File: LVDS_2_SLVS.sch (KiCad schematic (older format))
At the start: 6 parts

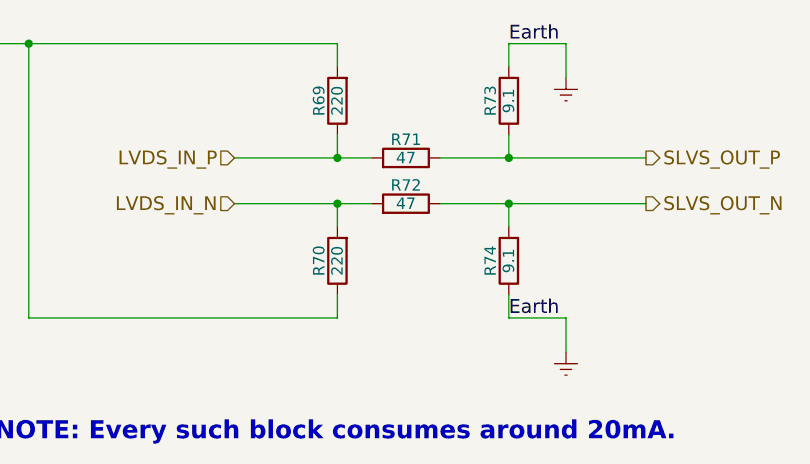
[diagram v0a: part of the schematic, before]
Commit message: Adding more LVDS lines
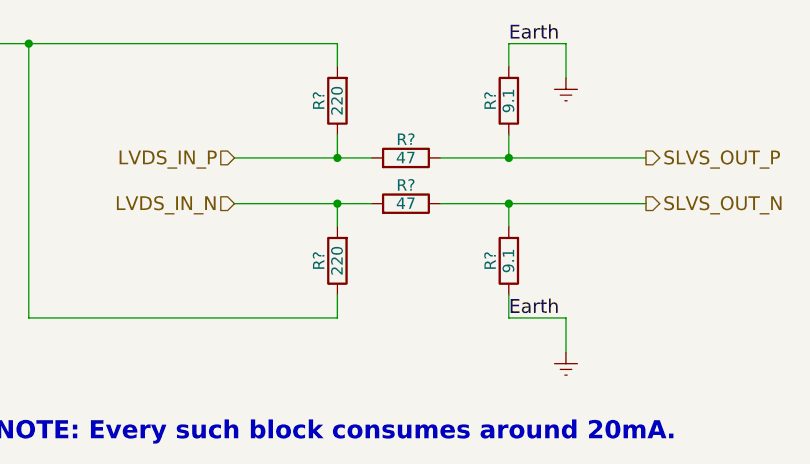
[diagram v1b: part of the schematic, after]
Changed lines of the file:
@@
 $Descr A4 11693 8268
 encoding utf-8
-Sheet 10 12
+Sheet 10 19
 Title ""
 Date ""
@@
 AR Path="/6191D89C/63D3885E/5955E861" Ref="R63"  Part="1"
 AR Path="/6191D89C/63D47A03/5955E861" Ref="R69"  Part="1"
-F 0 "R69" V 2680 1250 50  0000 C CNN
+AR Path="/6366AF3A/63C53CD1/5955E861" Ref="R?"  Part="1"
+AR Path="/6366AF3A/63D0A579/5955E861" Ref="R?"  Part="1"
+AR Path="/6366AF3A/63D1A4B4/5955E861" Ref="R?"  Part="1"
+AR Path="/6366AF3A/63D296AD/5955E861" Ref="R?"  Part="1"
+AR Path="/6366AF3A/63D3885E/5955E861" Ref="R?"  Part="1"
+AR Path="/6366AF3A/63D47A03/5955E861" Ref="R?"  Part="1"
+F 0 "R?" V 2680 1250 50  0000 C CNN
 F 1 "220" V 2600 1250 50  0000 C CNN
 F 2 "Resistors_SMD:R_0603" V 2530 1250 50  0001 C CNN
@@
 AR Path="/6191D89C/63D3885E/5955F5C4" Ref="R66"  Part="1"
 AR Path="/6191D89C/63D47A03/5955F5C4" Ref="R72"  Part="1"
-F 0 "R72" V 2980 1700 50  0000 C CNN
+AR Path="/6366AF3A/63C53CD1/5955F5C4" Ref="R?"  Part="1"
+AR Path="/6366AF3A/63D0A579/5955F5C4" Ref="R?"  Part="1"
+AR Path="/6366AF3A/63D1A4B4/5955F5C4" Ref="R?"  Part="1"
+AR Path="/6366AF3A/63D296AD/5955F5C4" Ref="R?"  Part="1"
+AR Path="/6366AF3A/63D3885E/5955F5C4" Ref="R?"  Part="1"
+AR Path="/6366AF3A/63D47A03/5955F5C4" Ref="R?"  Part="1"
+F 0 "R?" V 2980 1700 50  0000 C CNN
 F 1 "47" V 2900 1700 50  0000 C CNN
 F 2 "Resistors_SMD:R_0603" V 2830 1700 50  0001 C CNN
@@
 AR Path="/6191D89C/63D3885E/61C6D193" Ref="#PWR0125"  Part="1"
 AR Path="/6191D89C/63D47A03/61C6D193" Ref="#PWR0127"  Part="1"
-F 0 "#PWR0127" H 3600 2100 50  0001 C CNN
+AR Path="/6366AF3A/63C53CD1/61C6D193" Ref="#PWR?"  Part="1"
+AR Path="/6366AF3A/63D0A579/61C6D193" Ref="#PWR?"  Part="1"
+AR Path="/6366AF3A/63D1A4B4/61C6D193" Ref="#PWR?"  Part="1"
+AR Path="/6366AF3A/63D296AD/61C6D193" Ref="#PWR?"  Part="1"
+AR Path="/6366AF3A/63D3885E/61C6D193" Ref="#PWR?"  Part="1"
+AR Path="/6366AF3A/63D47A03/61C6D193" Ref="#PWR?"  Part="1"
+F 0 "#PWR?" H 3600 2100 50  0001 C CNN
 F 1 "Earth" H 3600 2200 50  0001 C CNN
 F 2 "" H 3600 2350 50  0000 C CNN
@@
 AR Path="/6191D89C/63D3885E/61C6D191" Ref="#PWR0126"  Part="1"
 AR Path="/6191D89C/63D47A03/61C6D191" Ref="#PWR0128"  Part="1"
-F 0 "#PWR0128" H 3600 900 50  0001 C CNN
+AR Path="/6366AF3A/63C53CD1/61C6D191" Ref="#PWR?"  Part="1"
+AR Path="/6366AF3A/63D0A579/61C6D191" Ref="#PWR?"  Part="1"
+AR Path="/6366AF3A/63D1A4B4/61C6D191" Ref="#PWR?"  Part="1"
+AR Path="/6366AF3A/63D296AD/61C6D191" Ref="#PWR?"  Part="1"
+AR Path="/6366AF3A/63D3885E/61C6D191" Ref="#PWR?"  Part="1"
+AR Path="/6366AF3A/63D47A03/61C6D191" Ref="#PWR?"  Part="1"
+F 0 "#PWR?" H 3600 900 50  0001 C CNN
 F 1 "Earth" H 3600 1000 50  0001 C CNN
 F 2 "" H 3600 1150 50  0000 C CNN
@@
 AR Path="/6191D89C/63D3885E/61C6D194" Ref="R64"  Part="1"
 AR Path="/6191D89C/63D47A03/61C6D194" Ref="R70"  Part="1"
-F 0 "R70" V 2680 1950 50  0000 C CNN
+AR Path="/6366AF3A/63C53CD1/61C6D194" Ref="R?"  Part="1"
+AR Path="/6366AF3A/63D0A579/61C6D194" Ref="R?"  Part="1"
+AR Path="/6366AF3A/63D1A4B4/61C6D194" Ref="R?"  Part="1"
+AR Path="/6366AF3A/63D296AD/61C6D194" Ref="R?"  Part="1"
+AR Path="/6366AF3A/63D3885E/61C6D194" Ref="R?"  Part="1"
+AR Path="/6366AF3A/63D47A03/61C6D194" Ref="R?"  Part="1"
+F 0 "R?" V 2680 1950 50  0000 C CNN
 F 1 "220" V 2600 1950 50  0000 C CNN
 F 2 "Resistors_SMD:R_0603" V 2530 1950 50  0001 C CNN
@@
 AR Path="/6191D89C/63D3885E/61C6D195" Ref="R65"  Part="1"
 AR Path="/6191D89C/63D47A03/61C6D195" Ref="R71"  Part="1"
-F 0 "R71" V 2980 1500 50  0000 C CNN
+AR Path="/6366AF3A/63C53CD1/61C6D195" Ref="R?"  Part="1"
+AR Path="/6366AF3A/63D0A579/61C6D195" Ref="R?"  Part="1"
+AR Path="/6366AF3A/63D1A4B4/61C6D195" Ref="R?"  Part="1"
+AR Path="/6366AF3A/63D296AD/61C6D195" Ref="R?"  Part="1"
+AR Path="/6366AF3A/63D3885E/61C6D195" Ref="R?"  Part="1"
+AR Path="/6366AF3A/63D47A03/61C6D195" Ref="R?"  Part="1"
+F 0 "R?" V 2980 1500 50  0000 C CNN
 F 1 "47" V 2900 1500 50  0000 C CNN
 F 2 "Resistors_SMD:R_0603" V 2830 1500 50  0001 C CNN
@@
 AR Path="/6191D89C/63D3885E/5955E920" Ref="R67"  Part="1"
 AR Path="/6191D89C/63D47A03/5955E920" Ref="R73"  Part="1"
-F 0 "R73" V 3430 1250 50  0000 C CNN
+AR Path="/6366AF3A/63C53CD1/5955E920" Ref="R?"  Part="1"
+AR Path="/6366AF3A/63D0A579/5955E920" Ref="R?"  Part="1"
+AR Path="/6366AF3A/63D1A4B4/5955E920" Ref="R?"  Part="1"
+AR Path="/6366AF3A/63D296AD/5955E920" Ref="R?"  Part="1"
+AR Path="/6366AF3A/63D3885E/5955E920" Ref="R?"  Part="1"
+AR Path="/6366AF3A/63D47A03/5955E920" Ref="R?"  Part="1"
+F 0 "R?" V 3430 1250 50  0000 C CNN
 F 1 "9.1" V 3350 1250 50  0000 C CNN
 F 2 "Resistors_SMD:R_0603_HandSoldering" V 3280 1250 50  0001 C CNN
@@
 AR Path="/6191D89C/63D3885E/63C11627" Ref="R68"  Part="1"
 AR Path="/6191D89C/63D47A03/63C11627" Ref="R74"  Part="1"
-F 0 "R74" V 3430 1950 50  0000 C CNN
+AR Path="/6366AF3A/63C53CD1/63C11627" Ref="R?"  Part="1"
+AR Path="/6366AF3A/63D0A579/63C11627" Ref="R?"  Part="1"
+AR Path="/6366AF3A/63D1A4B4/63C11627" Ref="R?"  Part="1"
+AR Path="/6366AF3A/63D296AD/63C11627" Ref="R?"  Part="1"
+AR Path="/6366AF3A/63D3885E/63C11627" Ref="R?"  Part="1"
+AR Path="/6366AF3A/63D47A03/63C11627" Ref="R?"  Part="1"
+F 0 "R?" V 3430 1950 50  0000 C CNN
 F 1 "9.1" V 3350 1950 50  0000 C CNN
 F 2 "Resistors_SMD:R_0603_HandSoldering" V 3280 1950 50  0001 C CNN

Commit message: added 4 bit level shifter VADJ to 3.3 volt
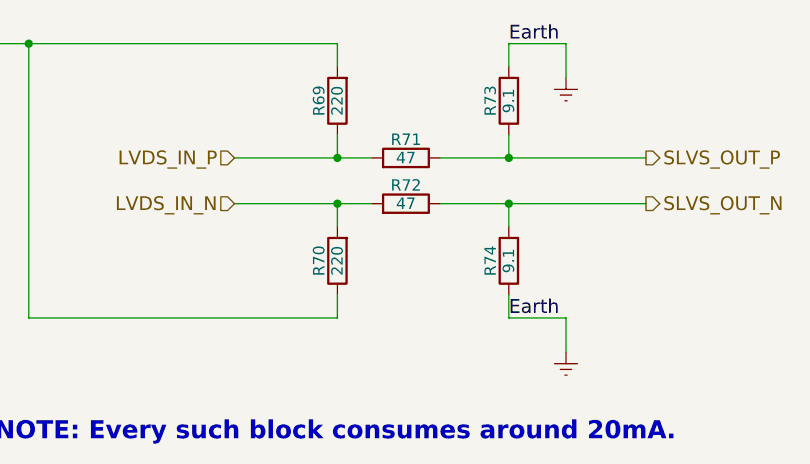
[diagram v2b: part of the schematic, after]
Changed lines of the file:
@@
 $Descr A4 11693 8268
 encoding utf-8
-Sheet 10 19
+Sheet 6 12
 Title ""
 Date ""
@@
 AR Path="/6366AF3A/63D3885E/5955E861" Ref="R?"  Part="1"
 AR Path="/6366AF3A/63D47A03/5955E861" Ref="R?"  Part="1"
-F 0 "R?" V 2680 1250 50  0000 C CNN
+F 0 "R69" V 2680 1250 50  0000 C CNN
 F 1 "220" V 2600 1250 50  0000 C CNN
 F 2 "Resistors_SMD:R_0603" V 2530 1250 50  0001 C CNN
@@
 AR Path="/6366AF3A/63D3885E/5955F5C4" Ref="R?"  Part="1"
 AR Path="/6366AF3A/63D47A03/5955F5C4" Ref="R?"  Part="1"
-F 0 "R?" V 2980 1700 50  0000 C CNN
+F 0 "R72" V 2980 1700 50  0000 C CNN
 F 1 "47" V 2900 1700 50  0000 C CNN
 F 2 "Resistors_SMD:R_0603" V 2830 1700 50  0001 C CNN
@@
 AR Path="/6366AF3A/63D3885E/61C6D193" Ref="#PWR?"  Part="1"
 AR Path="/6366AF3A/63D47A03/61C6D193" Ref="#PWR?"  Part="1"
-F 0 "#PWR?" H 3600 2100 50  0001 C CNN
+F 0 "#PWR0127" H 3600 2100 50  0001 C CNN
 F 1 "Earth" H 3600 2200 50  0001 C CNN
 F 2 "" H 3600 2350 50  0000 C CNN
@@
 AR Path="/6366AF3A/63D3885E/61C6D191" Ref="#PWR?"  Part="1"
 AR Path="/6366AF3A/63D47A03/61C6D191" Ref="#PWR?"  Part="1"
-F 0 "#PWR?" H 3600 900 50  0001 C CNN
+F 0 "#PWR0128" H 3600 900 50  0001 C CNN
 F 1 "Earth" H 3600 1000 50  0001 C CNN
 F 2 "" H 3600 1150 50  0000 C CNN
@@
 AR Path="/6366AF3A/63D3885E/61C6D194" Ref="R?"  Part="1"
 AR Path="/6366AF3A/63D47A03/61C6D194" Ref="R?"  Part="1"
-F 0 "R?" V 2680 1950 50  0000 C CNN
+F 0 "R70" V 2680 1950 50  0000 C CNN
 F 1 "220" V 2600 1950 50  0000 C CNN
 F 2 "Resistors_SMD:R_0603" V 2530 1950 50  0001 C CNN
@@
 AR Path="/6366AF3A/63D3885E/61C6D195" Ref="R?"  Part="1"
 AR Path="/6366AF3A/63D47A03/61C6D195" Ref="R?"  Part="1"
-F 0 "R?" V 2980 1500 50  0000 C CNN
+F 0 "R71" V 2980 1500 50  0000 C CNN
 F 1 "47" V 2900 1500 50  0000 C CNN
 F 2 "Resistors_SMD:R_0603" V 2830 1500 50  0001 C CNN
@@
 AR Path="/6366AF3A/63D3885E/5955E920" Ref="R?"  Part="1"
 AR Path="/6366AF3A/63D47A03/5955E920" Ref="R?"  Part="1"
-F 0 "R?" V 3430 1250 50  0000 C CNN
+F 0 "R73" V 3430 1250 50  0000 C CNN
 F 1 "9.1" V 3350 1250 50  0000 C CNN
 F 2 "Resistors_SMD:R_0603_HandSoldering" V 3280 1250 50  0001 C CNN
@@
 AR Path="/6366AF3A/63D3885E/63C11627" Ref="R?"  Part="1"
 AR Path="/6366AF3A/63D47A03/63C11627" Ref="R?"  Part="1"
-F 0 "R?" V 3430 1950 50  0000 C CNN
+F 0 "R74" V 3430 1950 50  0000 C CNN
 F 1 "9.1" V 3350 1950 50  0000 C CNN
 F 2 "Resistors_SMD:R_0603_HandSoldering" V 3280 1950 50  0001 C CNN
